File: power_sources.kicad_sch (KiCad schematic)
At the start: 24 parts, among them J3 ESC pads (CURR TX M4 M3 M2 M1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, J4 USB_C_PROGRAM_POWER, U25 TPS2121RUXR, U26 AP63205WU-7

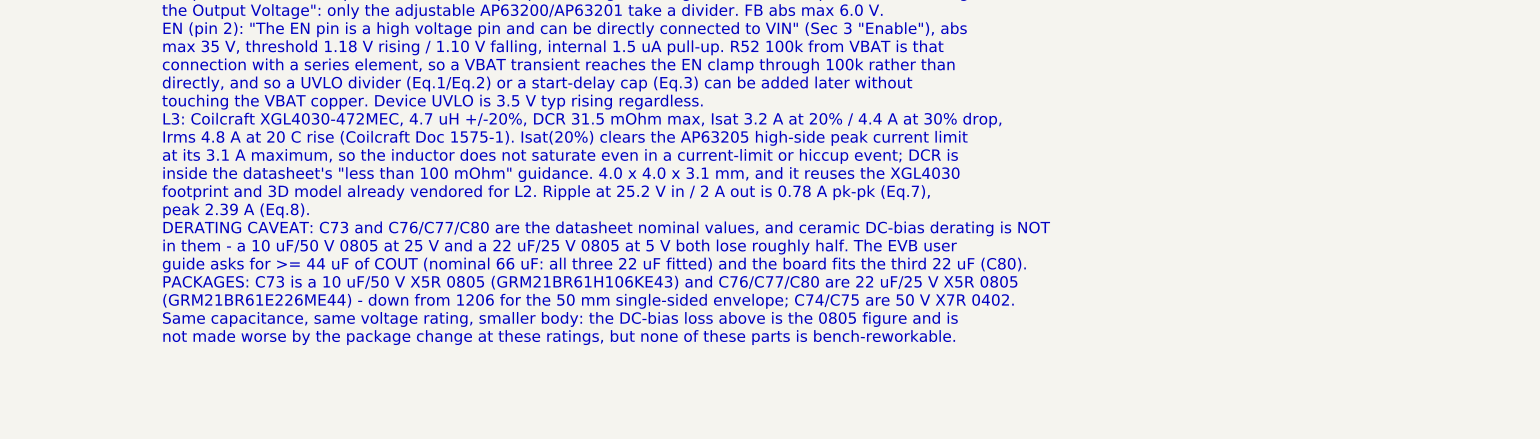
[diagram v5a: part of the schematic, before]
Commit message: Flash-socket caps back on the front, minimal socket silk; L2 to XGL3020-222
C62/C63 (U24 decoupling) are fitted on the front again, so a user adding a
flash or PSRAM chip to the back-side SOIC-8 socket only solders the chip;
the back legend is reduced to "FLASH" / "SOIC-8" plus the pin-1 mark, and
the compatible parts (150-mil SOIC-8 QSPI NOR: W25Q16/32/64JVSS, GD25Q32C/
64C, MX25L3233F/6433F; QSPI PSRAM: APS6404L-3SQR-SN, ESP-PSRAM64H, IPS6404L,
LY68L6400) are documented in DESIGN_SPEC/LIBRARIES.

L2 (TPS62913 3.3 V buck inductor) shrinks from XGL4030-222 (4x4x3.1) to
Coilcraft XGL3020-222MEC (3x3x2.0; Isat 2.2 A @20 %, 2.85 A @30 %, DCR
30.5 mOhm, Doc 1776 Rev 02/19/26) against a ~0.95 A peak; project footprint
from the Coilcraft land pattern, vendor STEP aligned and verified against
copper. L3 stays XGL4030-472: its floor is the AP63205's 3.1 A current-limit
ceiling and the XGL4020 shares the 4x4 land pattern. Board 46.6 x 41.2 mm;
DRC unrouted-only; ERC 0/0, checker PASS, ngspice PASS, audit 140/140.

Co-Authored-By: Claude Fable 5.1 <noreply@anthropic.com>
Claude-Session: https://claude.ai/code/session_01U6Ud7JA3CDTJZVcZZr5sx1
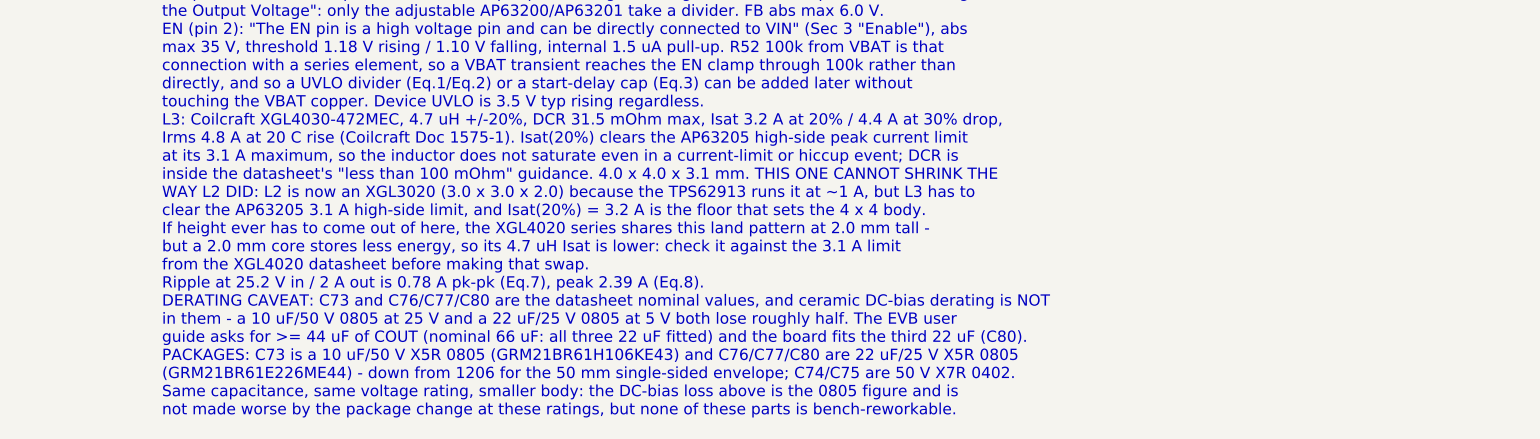
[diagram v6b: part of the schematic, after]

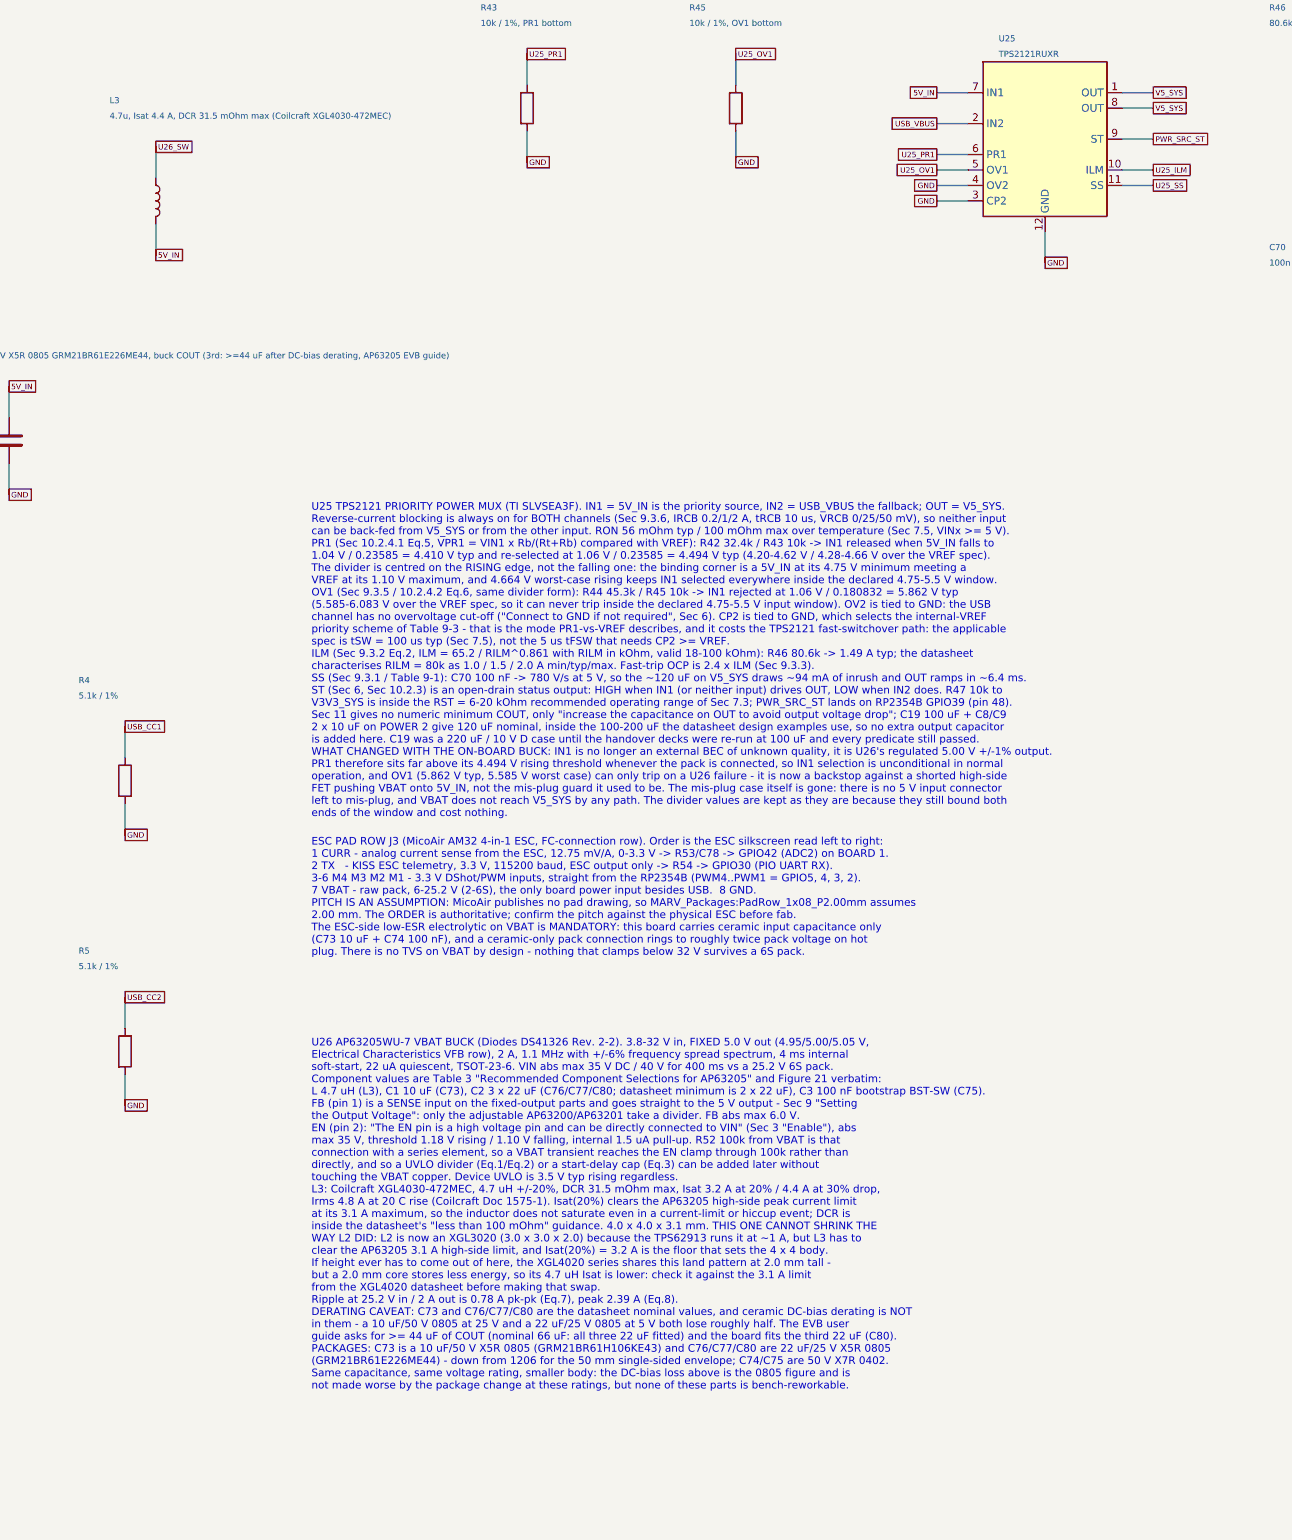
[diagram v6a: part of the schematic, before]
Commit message: JLCPCB sourcing: Basic-part refactor, LCSC numbers in the schematic, order files and audit
Parts audited line by line against JLCPCB's live catalogue (tools/jlc/,
reports/jlc-audit.md). Resistors move 0201 -> 0402 (JLC's Basic library has
no 0201 resistor), the U7 FB divider becomes 10k/3.16k 0.1 % (15.8k 0.1 % is
not stocked), Y1 becomes TAXM12M4RFBCCT2T (CL 12 pF) with 18 pF loads, L2/L3
become CJIANG FTC303020D2R2MBCA / FTC404030S4R7MGCA (stocked; Isat 5.5 A /
6.0 A at 30 %, footprints + models vendored from KiCad), the 22 uF/25 V and
10 uF lines move to Basic parts. The U24 default fit is W25Q32JVSNIQ (the
W25Q64JVSSIQ is a 208-mil part and never fitted the 150-mil socket).

Every fitted symbol carries a hidden LCSC property stamped from
tools/jlc/lcsc_map.csv; tools/jlc/export_jlc.py writes reports/jlc-bom.csv
and reports/jlc-cpl.csv (top-side SMT, headers unpopulated, U24 DNP).
Result: 46 unique parts, 16 Basic / 1 Preferred / 29 Extended (was 9/1/35),
extended-fee estimate $87 (was $105), $45.68 per board at 10 (was $52.97 with
L2 unsourced). DESIGN_SPEC gains a Manufacturing (JLCPCB) section with the
quote parameters. Board rebuilt (0 fit/geometry, DRC unrouted-only); ERC
0/0, checker PASS, ngspice PASS, audit 140/140.

Co-Authored-By: Claude Fable 5.1 <noreply@anthropic.com>
Claude-Session: https://claude.ai/code/session_01U6Ud7JA3CDTJZVcZZr5sx1
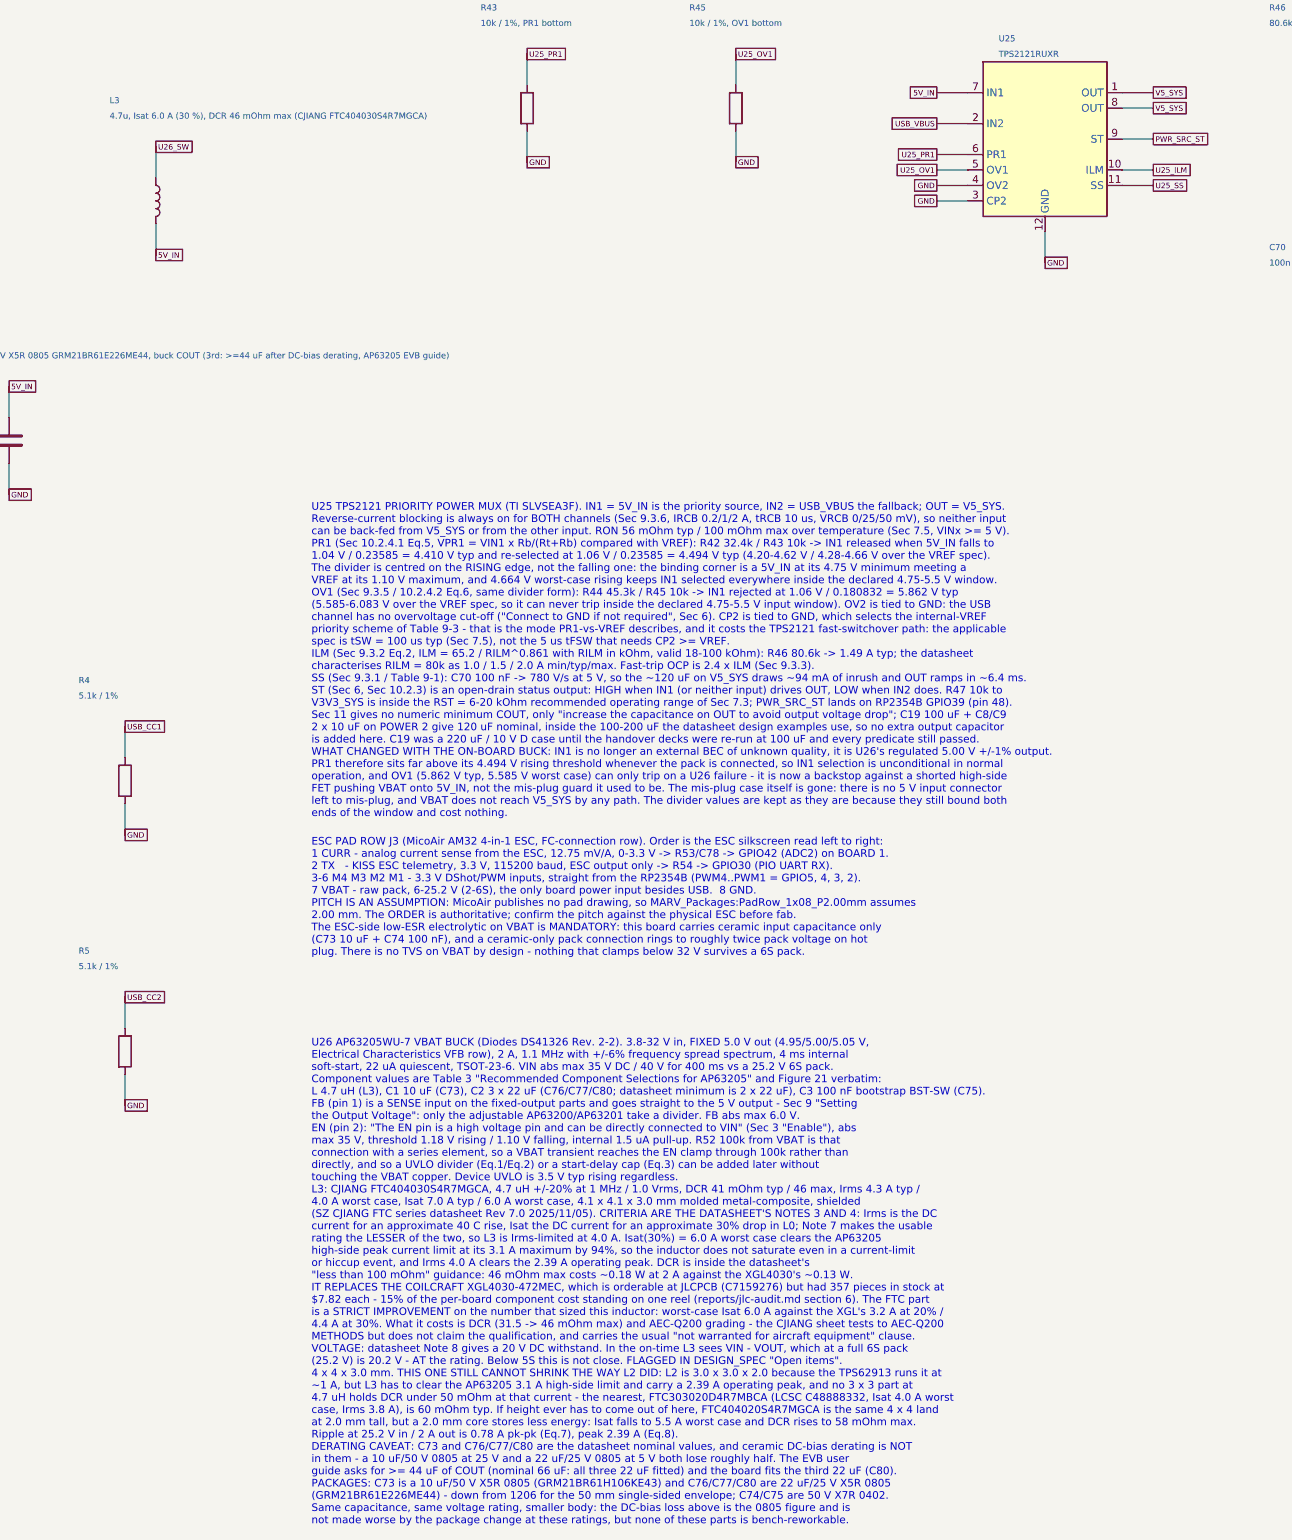
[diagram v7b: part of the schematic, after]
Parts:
- C7: LCSC (none) -> C52923
- C70, C71, C72: LCSC (none) -> C1525
- C73: LCSC (none) -> C440198
- C74, C75: LCSC (none) -> C307331
- C76, C77, C80: LCSC (none) -> C45783
- J4: LCSC (none) -> C165948
- L3: value 4.7u, Isat 4.4 A, DCR 31.5 mOhm max (Coilcraft XGL4030-472MEC) -> 4.7u, Isat 6.0 A (30 %), DCR 46 mOhm max (CJIANG FTC404030S4R7MGCA); footprint MARV_Packages:L_Coilcraft_XxL4030 -> MARV_Packages:L_Changjiang_FTC404030S; LCSC (none) -> C39676083
- R4, R5: footprint Resistor_SMD:R_0201_0603Metric -> Resistor_SMD:R_0402_1005Metric; LCSC (none) -> C25905
- R42: footprint Resistor_SMD:R_0201_0603Metric -> Resistor_SMD:R_0402_1005Metric; LCSC (none) -> C22369333
- R43, R45, R47: footprint Resistor_SMD:R_0201_0603Metric -> Resistor_SMD:R_0402_1005Metric; LCSC (none) -> C25744
- R44: footprint Resistor_SMD:R_0201_0603Metric -> Resistor_SMD:R_0402_1005Metric; LCSC (none) -> C137977
- R46: footprint Resistor_SMD:R_0201_0603Metric -> Resistor_SMD:R_0402_1005Metric; LCSC (none) -> C2998147
- R52: footprint Resistor_SMD:R_0201_0603Metric -> Resistor_SMD:R_0402_1005Metric; LCSC (none) -> C25741
- U25: LCSC (none) -> C485916
- U26: LCSC (none) -> C2071056
